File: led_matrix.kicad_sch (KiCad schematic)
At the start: 119 parts, among them J1 I2C, J2 Extra, J3 Address, J4 +5V, J5 GND, J6 Power Input, J7 Columns, J8 Row Addr., J9 VCC, Q1 2N3904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

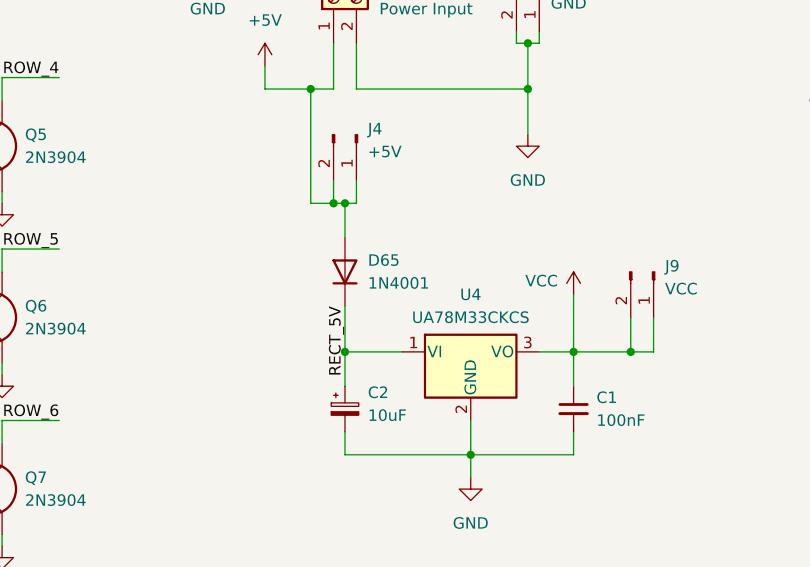
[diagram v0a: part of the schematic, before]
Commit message: Replace diode type with a schottky one
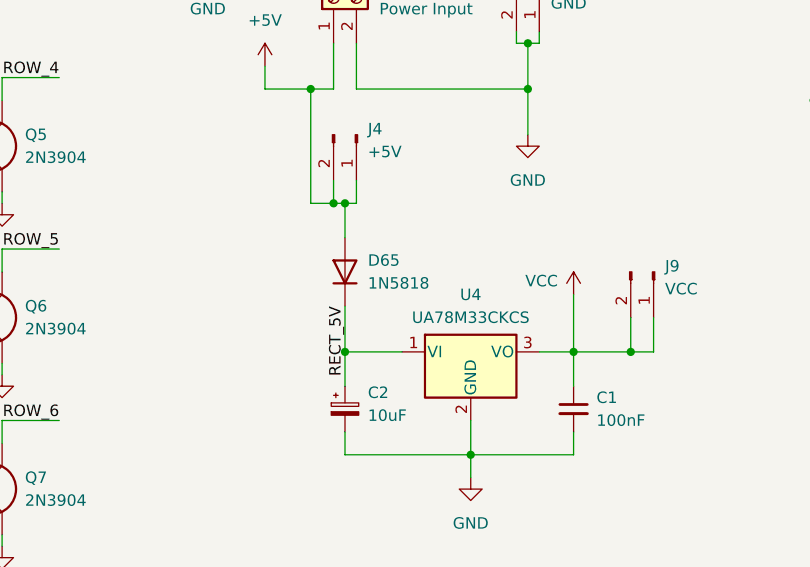
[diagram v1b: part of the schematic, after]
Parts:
- D65: value 1N4001 -> 1N5818
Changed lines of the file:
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@@
 			)
 		)
-		(property "Value" "1N4001"
+		(property "Value" "1N5818"
 			(at 132.08 142.2399 90)
 			(effects

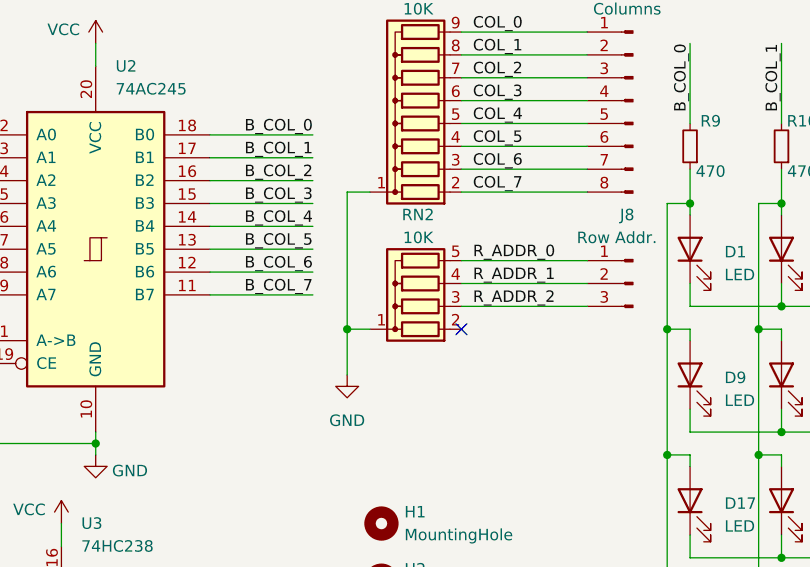
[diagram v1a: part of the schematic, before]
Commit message: Moved around some components
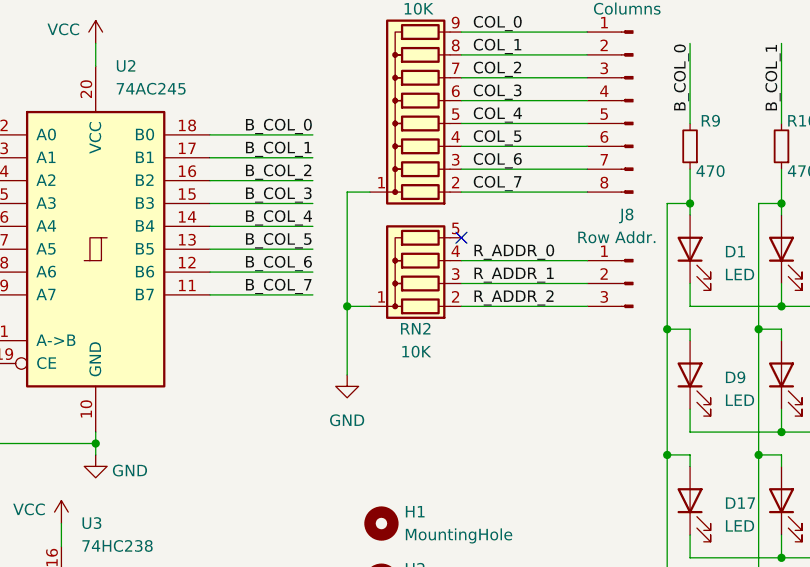
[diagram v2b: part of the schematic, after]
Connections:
- net R_ADDR_0: now also RN2.4 (R3); no longer RN2.5 (R4)
- net R_ADDR_1: now also RN2.3 (R2); no longer RN2.4 (R3)
- net R_ADDR_2: now also RN2.2 (R1); no longer RN2.3 (R2)
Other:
- moved on the sheet: RN2
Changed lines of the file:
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@@
 	)
 	(junction
+		(at 146.05 49.53)
+		(diameter 0)
+		(color 0 0 0 0)
+	)
+	(junction
 		(at 255.27 77.47)
 		(diameter 0)
@@
 	)
 	(junction
-		(at 146.05 52.07)
-		(diameter 0)
-		(color 0 0 0 0)
-	)
-	(junction
 		(at 49.53 97.79)
 		(diameter 0)
@@
 	)
 	(no_connect
-		(at 158.75 52.07)
+		(at 158.75 41.91)
 	)
 	(no_connect
@@
 	(wire
 		(pts
+			(xy 146.05 49.53) (xy 146.05 57.15)
+		)
+		(stroke
+			(width 0)
+			(type default)
+		)
+	)
+	(wire
+		(pts
 			(xy 201.93 52.07) (xy 204.47 52.07)
 		)
@@
 	(wire
 		(pts
-			(xy 146.05 57.15) (xy 146.05 52.07)
+			(xy 146.05 36.83) (xy 146.05 49.53)
 		)
 		(stroke
@@
 	(wire
 		(pts
-			(xy 146.05 52.07) (xy 148.59 52.07)
-		)
-		(stroke
-			(width 0)
-			(type default)
-		)
-	)
-	(wire
-		(pts
 			(xy 214.63 63.5) (xy 224.79 63.5)
 		)
@@
 	(wire
 		(pts
+			(xy 146.05 49.53) (xy 148.59 49.53)
+		)
+		(stroke
+			(width 0)
+			(type default)
+		)
+	)
+	(wire
+		(pts
 			(xy 245.11 77.47) (xy 255.27 77.47)
 		)
@@
 	(wire
 		(pts
-			(xy 146.05 52.07) (xy 146.05 36.83)
-		)
-		(stroke
-			(width 0)
-			(type default)
-		)
-	)
-	(wire
-		(pts
 			(xy 204.47 49.53) (xy 214.63 49.53)
 		)
@@
 	(symbol
 		(lib_id "Device:R_Network04")
-		(at 153.67 46.99 90)
+		(at 153.67 44.45 90)
 		(unit 1)
 		(exclude_from_sim no)
@@
 		(dnp no)
 		(property "Reference" "RN2"
-			(at 153.924 39.37 90)
+			(at 153.67 52.07 90)
 			(effects
 				(font
@@
 		)
 		(property "Value" "10K"
-			(at 153.924 41.91 90)
+			(at 153.67 54.61 90)
 			(effects
 				(font
@@
 		)
 		(property "Footprint" "Resistor_THT:R_Array_SIP5"
-			(at 153.67 40.005 90)
+			(at 153.67 37.465 90)
 			(effects
 				(font
@@
 		)
 		(property "Datasheet" "http://www.vishay.com/docs/31509/csc.pdf"
-			(at 153.67 46.99 0)
+			(at 153.67 44.45 0)
 			(effects
 				(font
@@
 		)
 		(property "Description" "4 resistor network, star topology, bussed resistors, small symbol"
-			(at 153.67 46.99 0)
+			(at 153.67 44.45 0)
 			(effects
 				(font

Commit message: Updated readme
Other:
- title: (none) -> 8x8 LED MATRIX EDUBOARD
- moved on the sheet: D1, D10, D11, D12, D13, D14, D15, D16, D17, D18, D19, D2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
